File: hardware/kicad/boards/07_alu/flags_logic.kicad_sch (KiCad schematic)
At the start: 14 parts, among them U16 74ACT151, U36 74HC86, U37 74LS08, U38 74LS540, U4 74HC688, U40 74LS377, U6 74HC688

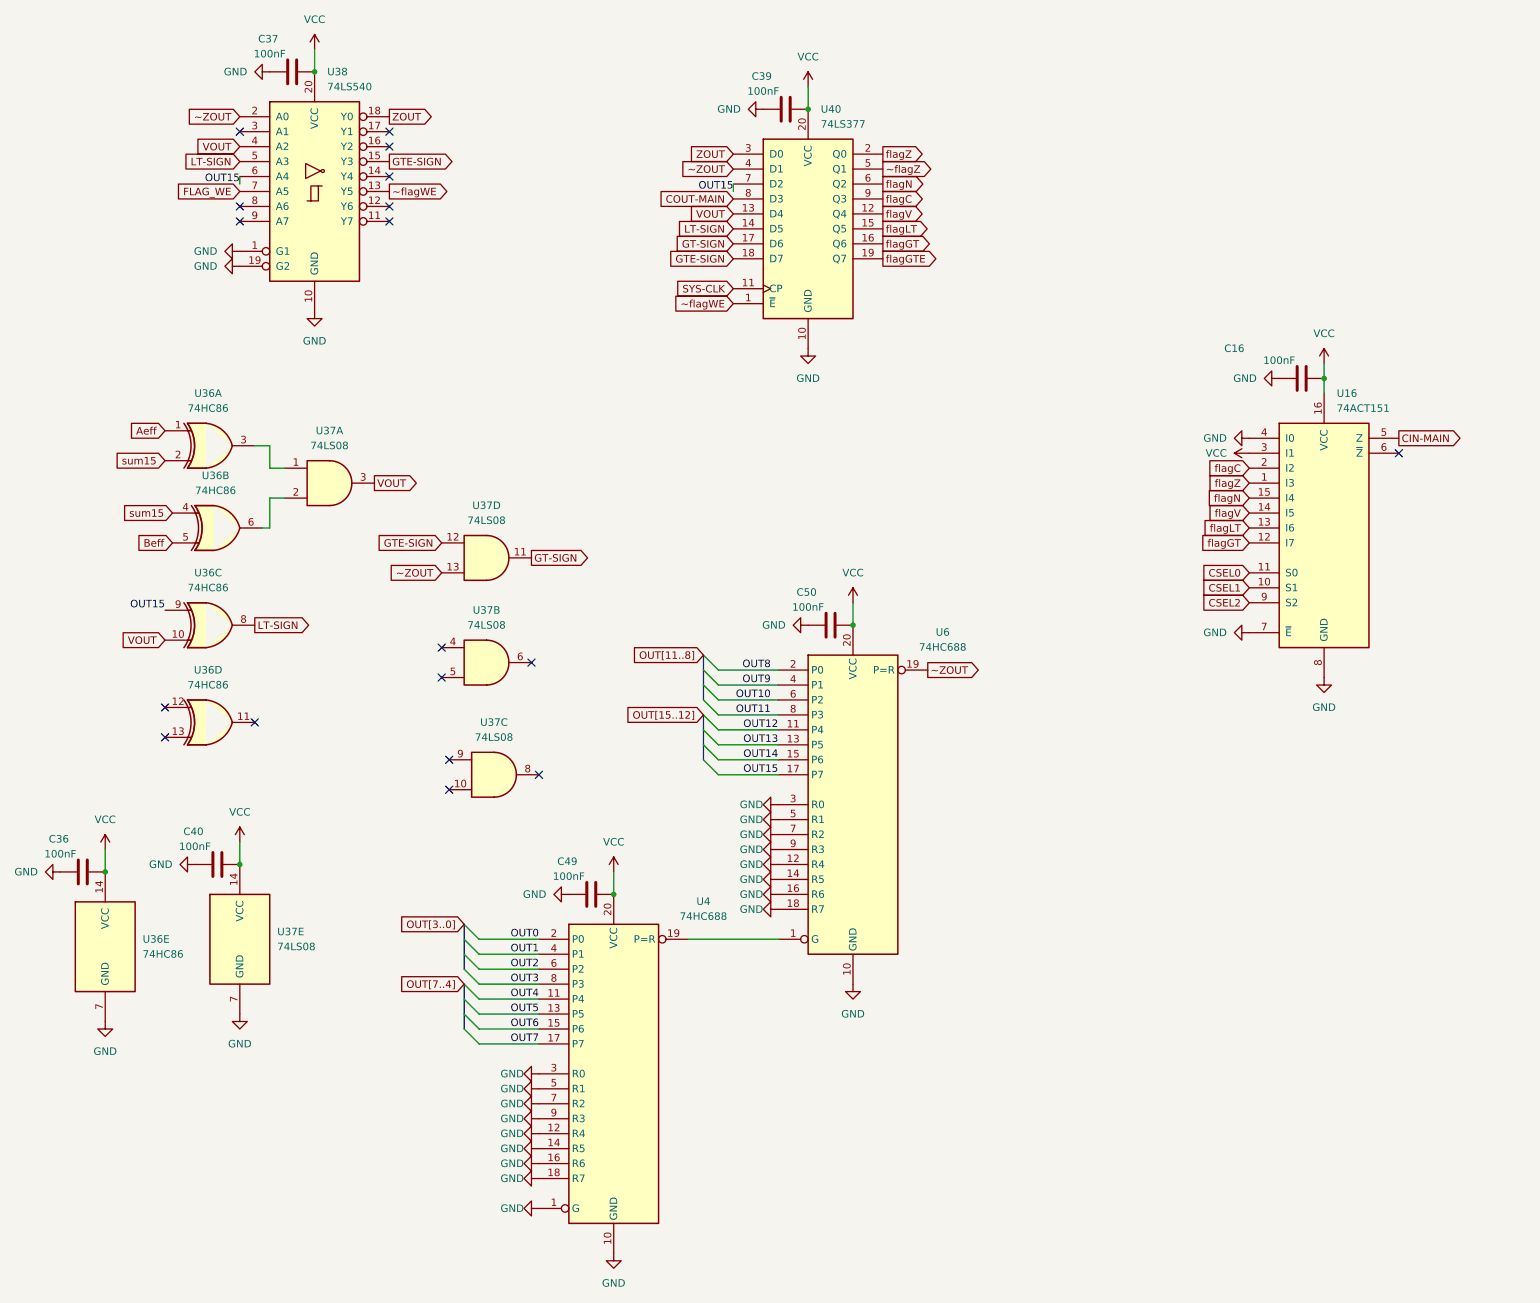
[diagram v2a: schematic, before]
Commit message: fix: resolved kicad erc tests to 0
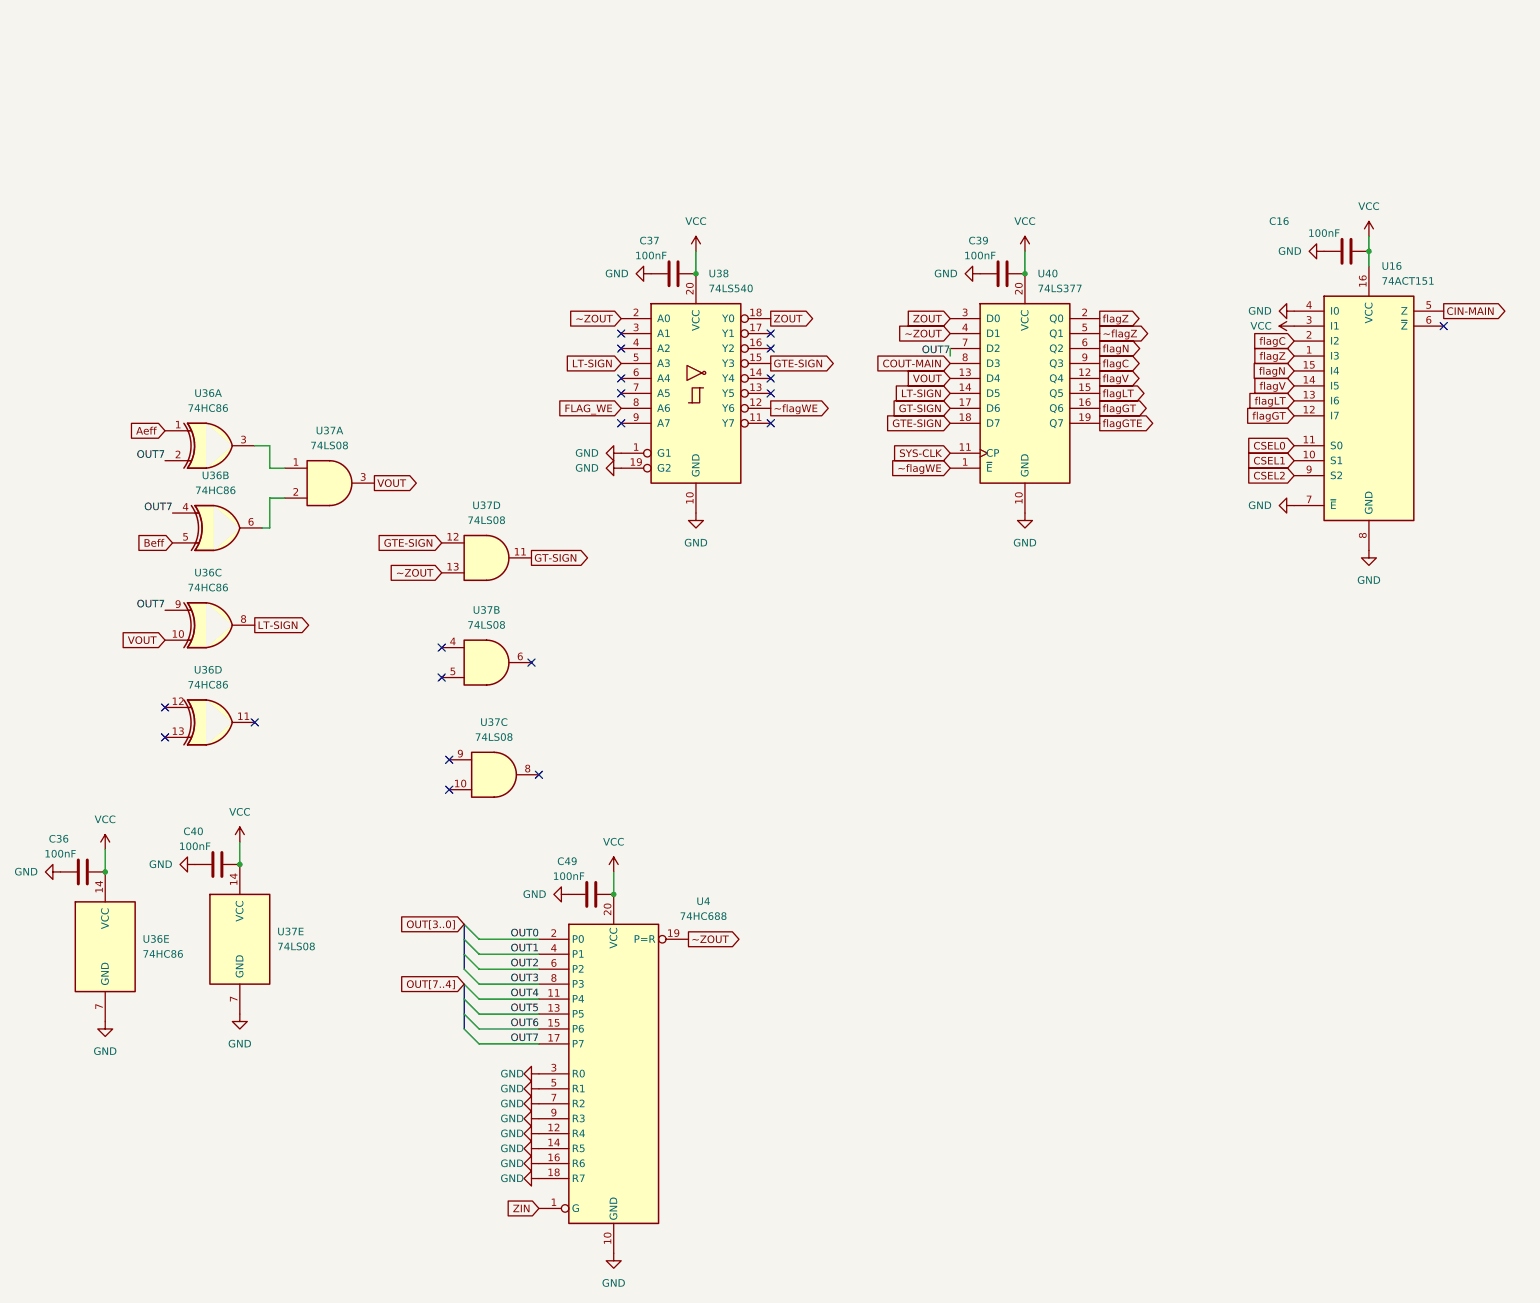
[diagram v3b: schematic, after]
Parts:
- removed C50: 100nF, Capacitor_SMD:C_0603_1608Metric, symbol Device:C
- removed U6: 74HC688, Package_SO:SOIC-20W_7.5x12.8mm_P1.27mm, symbol 74xx:74HC688
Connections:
- net sum15 is gone; now on net OUT7: U36.2, U36.4
- net FLAG_WE: now also U38.8 (A6); no longer U38.7 (A5)
- net GND: no longer U4.1 (G)
- net OUT7: now also U36.9, U40.7 (D2)
- net VOUT: no longer U38.4 (A2)
- net ~ZOUT: now also U4.19 (P=R)
- net ~flagWE: now also U38.12 (Y6); no longer U38.13 (Y5)
- removed net OUT15: U36.9, U38.6 (A4), U40.7 (D2)
- new net ZIN: U4.1 (G)
- no-connect marks 18 -> 20
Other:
- moved on the sheet: C16, C37, C39, U16, U38, U40

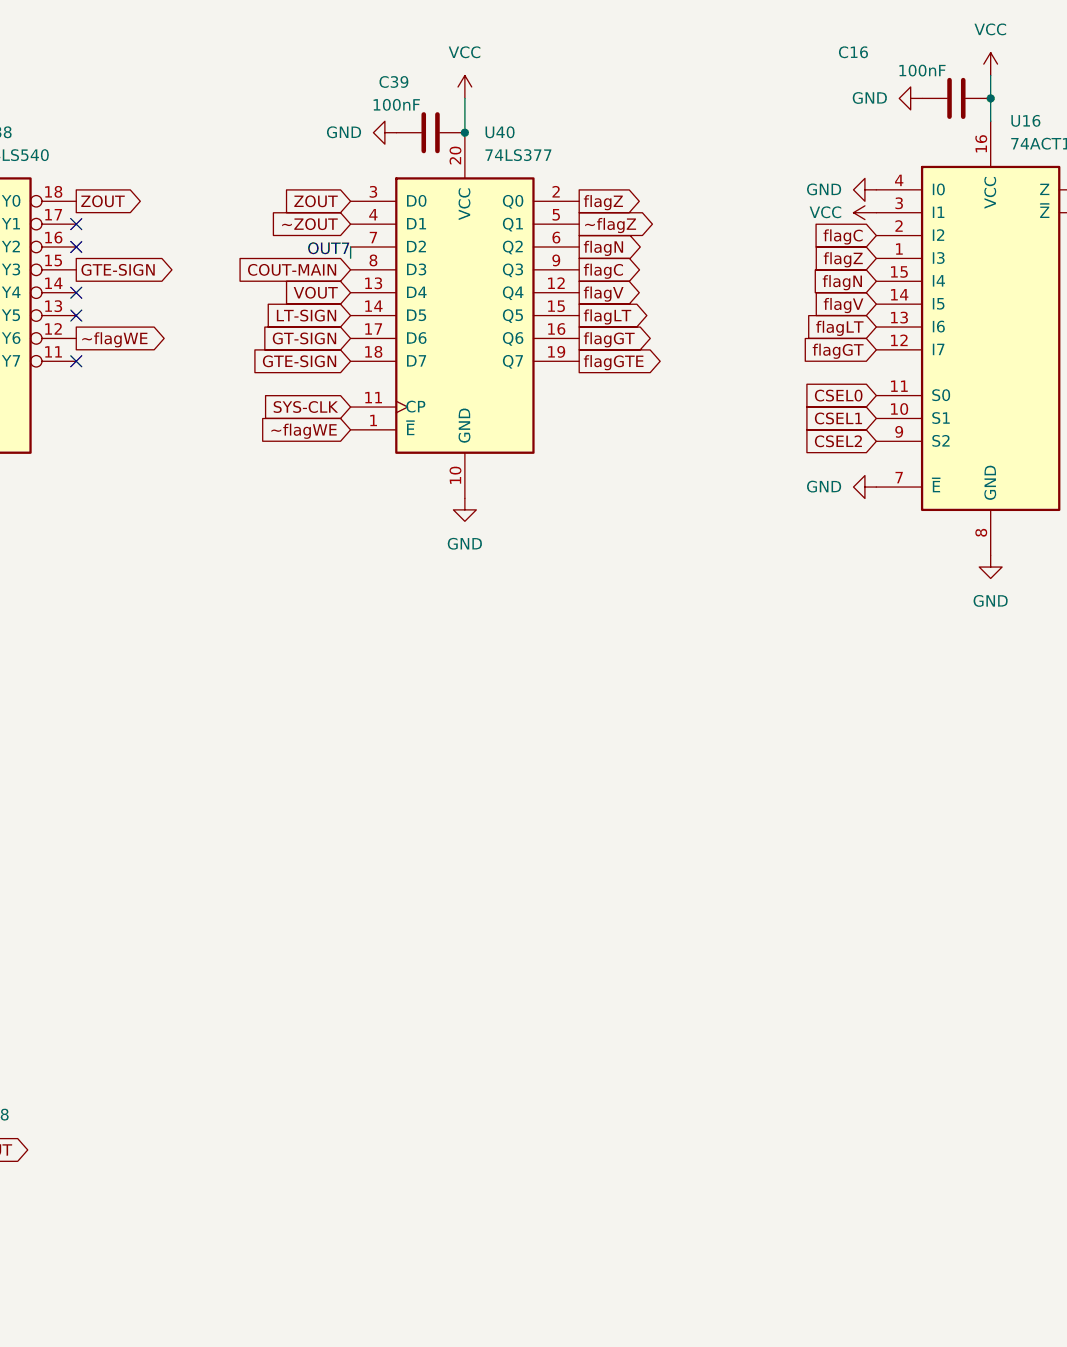
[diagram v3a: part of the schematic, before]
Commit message: checkpoint: routing flags and finishing final traces before pcb annotations and text
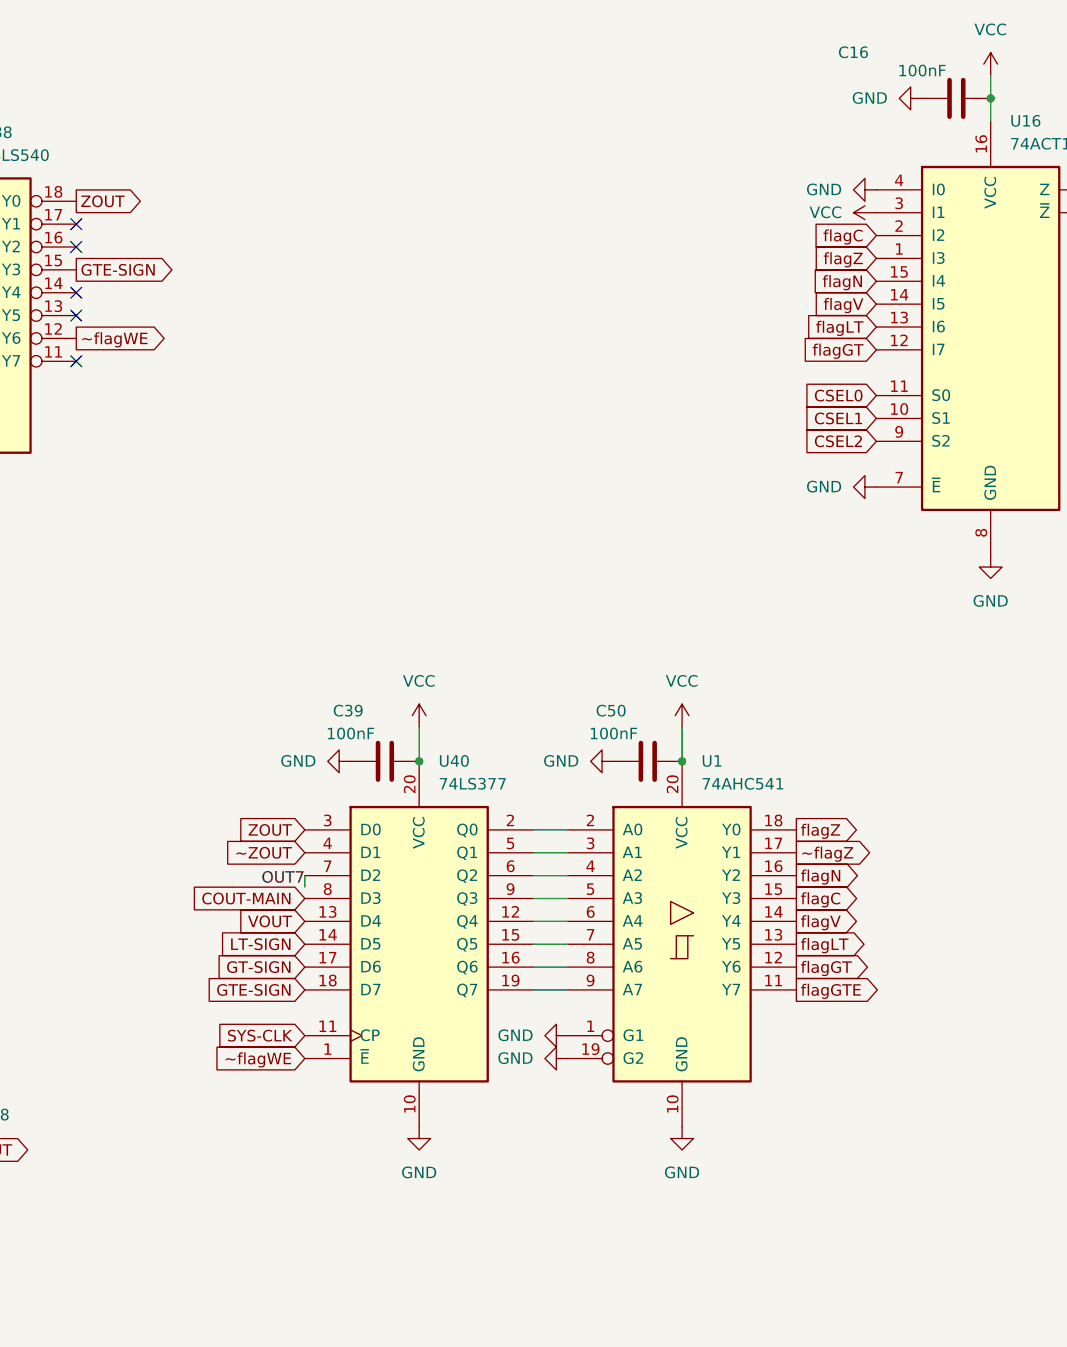
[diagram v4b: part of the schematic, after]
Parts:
- added C50: 100nF, Capacitor_SMD:C_0603_1608Metric, symbol Device:C
- added U1: 74AHC541, Package_SO:SOIC-20W_7.5x12.8mm_P1.27mm, symbol 74xx:74AHC541
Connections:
- net GND: now also C50.1, U1.1 (G1), U1.10 (GND), U1.19 (G2)
- net VCC: now also C50.2, U1.20 (VCC)
- net flagC: now also U1.15 (Y3); no longer U40.9 (Q3)
- net flagGT: now also U1.12 (Y6); no longer U40.16 (Q6)
- net flagGTE: now also U1.11 (Y7); no longer U40.19 (Q7)
- net flagLT: now also U1.13 (Y5); no longer U40.15 (Q5)
- net flagN: now also U1.16 (Y2); no longer U40.6 (Q2)
- net flagV: now also U1.14 (Y4); no longer U40.12 (Q4)
- net flagZ: now also U1.18 (Y0); no longer U40.2 (Q0)
- net ~flagZ: now also U1.17 (Y1); no longer U40.5 (Q1)
- new net: U1.6 (A4), U40.12 (Q4)
- new net: U1.7 (A5), U40.15 (Q5)
- new net: U1.8 (A6), U40.16 (Q6)
- new net: U1.9 (A7), U40.19 (Q7)
- new net: U1.2 (A0), U40.2 (Q0)
- new net: U1.3 (A1), U40.5 (Q1)
- new net: U1.4 (A2), U40.6 (Q2)
- new net: U1.5 (A3), U40.9 (Q3)
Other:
- moved on the sheet: C39, U40
